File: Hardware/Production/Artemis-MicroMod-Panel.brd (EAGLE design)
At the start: 199.6 x 83.1 mm, 438 parts, among them J1 MICROMOD-2222, J10 MICROMOD-2222, J11 MICROMOD-2222, J12 MICROMOD-2222, J13 MICROMOD-2222, J14 MICROMOD-2222, J15 MICROMOD-2222, J16 MICROMOD-2222, J2 MICROMOD-2222, J3 MICROMOD-2222, J4 MICROMOD-2222, J5 MICROMOD-2222, J6 MICROMOD-2222, J7 MICROMOD-2222, J8 MICROMOD-2222, J9 MICROMOD-2222, U1 ARTEMIS_MODULESMD, U10 CH340E_MSOP10, U11 ARTEMIS_MODULESMD, U12 CH340E_MSOP10, U13 ARTEMIS_MODULESMD, U14 CH340E_MSOP10, U15 ARTEMIS_MODULESMD, U16 CH340E_MSOP10, U17 ARTEMIS_MODULESMD, U18 CH340E_MSOP10, U19 ARTEMIS_MODULESMD, U2 ARTEMIS_MODULESMD, U20 CH340E_MSOP10, U21 ARTEMIS_MODULESMD, U22 CH340E_MSOP10, U23 ARTEMIS_MODULESMD, U24 CH340E_MSOP10, U25 ARTEMIS_MODULESMD, U26 CH340E_MSOP10, U27 ARTEMIS_MODULESMD, U28 CH340E_MSOP10, U29 ARTEMIS_MODULESMD, U3 CH340E_MSOP10, U30 CH340E_MSOP10, U31 ARTEMIS_MODULESMD, U32 CH340E_MSOP10, U4 ARTEMIS_MODULESMD, U5 CH340E_MSOP10, U6 CH340E_MSOP10, U7 ARTEMIS_MODULESMD, U8 CH340E_MSOP10, U9 ARTEMIS_MODULESMD, Y1 32.768kHz, Y10 32.768kHz, Y11 32.768kHz, Y12 32.768kHz, Y13 32.768kHz, Y14 32.768kHz, Y15 32.768kHz, Y16 32.768kHz, Y2 32.768kHz, Y3 32.768kHz, Y4 32.768kHz, Y5 32.768kHz, Y6 32.768kHz, Y7 32.768kHz, Y8 32.768kHz, Y9 32.768kHz

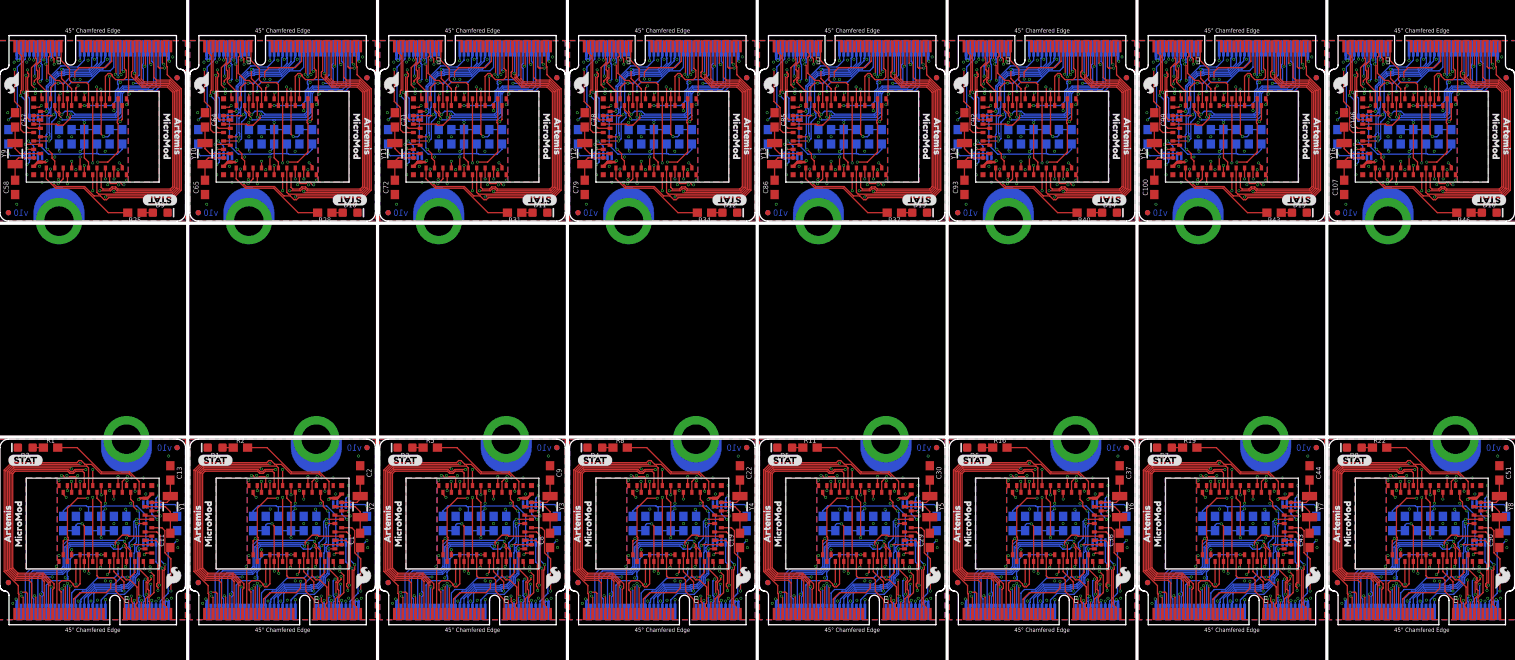
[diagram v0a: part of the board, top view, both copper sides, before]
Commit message: Adding panel files for v10
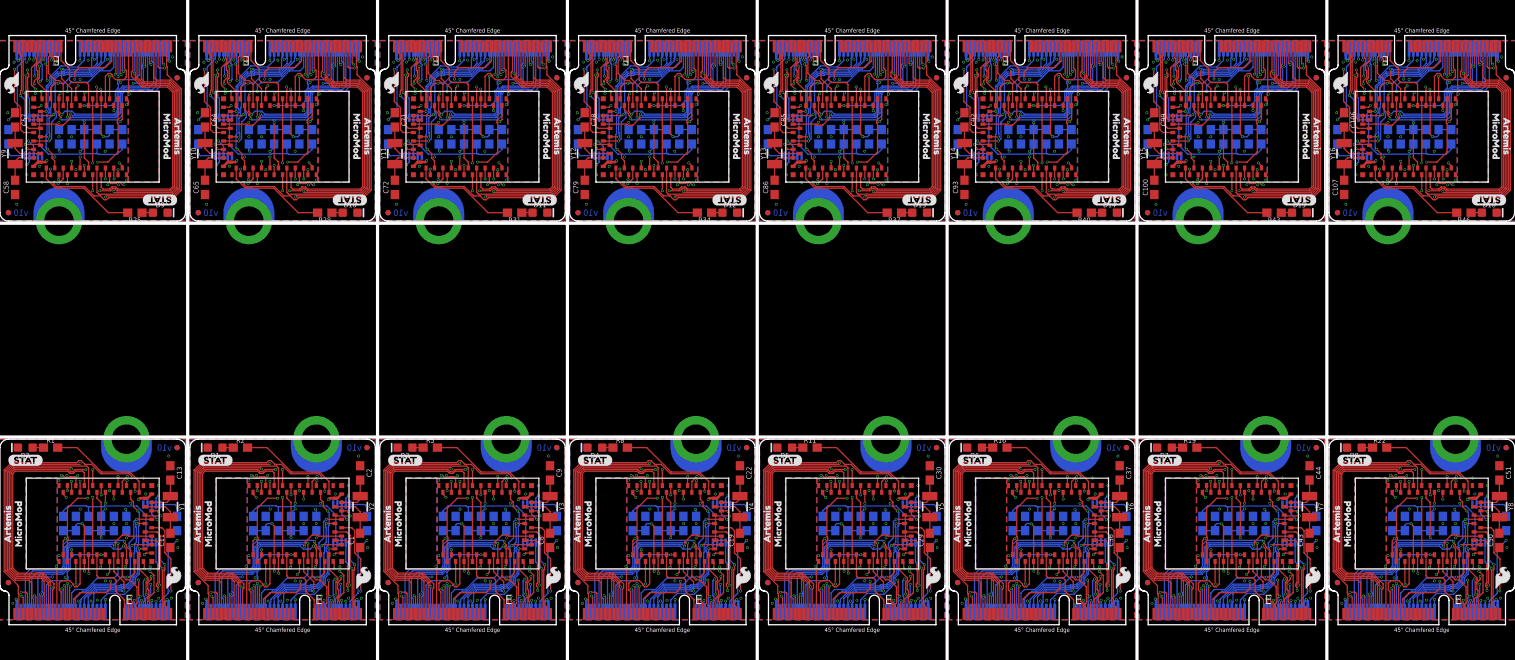
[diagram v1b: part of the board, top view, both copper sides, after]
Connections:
- net ADC_1ST renamed ADC0
- net ADC_1ST1 renamed ADC2
- net ADC_1ST10 renamed ADC20
- net ADC_1ST11 renamed ADC22
- net ADC_1ST12 renamed ADC24
- net ADC_1ST13 renamed ADC26
- net ADC_1ST14 renamed ADC28
- net ADC_1ST15 renamed ADC30
- net ADC_1ST2 renamed ADC4
- net ADC_1ST3 renamed ADC6
- net ADC_1ST4 renamed ADC8
- net ADC_1ST5 renamed ADC10
- net ADC_1ST6 renamed ADC12
- net ADC_1ST7 renamed ADC14
- net ADC_1ST8 renamed ADC16
- net ADC_1ST9 renamed ADC18
- net ADC_2ND renamed ADC1
- net ADC_2ND1 renamed ADC3
- net ADC_2ND10 renamed ADC21
- net ADC_2ND11 renamed ADC23
- net ADC_2ND12 renamed ADC25
- net ADC_2ND13 renamed ADC27
- net ADC_2ND14 renamed ADC29
- net ADC_2ND15 renamed ADC31
- net ADC_2ND2 renamed ADC5
- net ADC_2ND3 renamed ADC7
- net ADC_2ND4 renamed ADC9
- net ADC_2ND5 renamed ADC11
- net ADC_2ND6 renamed ADC13
- net ADC_2ND7 renamed ADC15
- net ADC_2ND8 renamed ADC17
- net ADC_2ND9 renamed ADC19
- net GPIO_1ST renamed D0
- net GPIO_1ST1 renamed D2
- net GPIO_1ST10 renamed D20
- net GPIO_1ST11 renamed D22
- net GPIO_1ST12 renamed D24
- net GPIO_1ST13 renamed D26
- net GPIO_1ST14 renamed D28
- net GPIO_1ST15 renamed D30
- net GPIO_1ST2 renamed D4
- net GPIO_1ST3 renamed D6
- net GPIO_1ST4 renamed D8
- net GPIO_1ST5 renamed D10
- net GPIO_1ST6 renamed D12
- net GPIO_1ST7 renamed D14
- net GPIO_1ST8 renamed D16
- net GPIO_1ST9 renamed D18
- net GPIO_2ND renamed D1
- net GPIO_2ND1 renamed D3
- net GPIO_2ND10 renamed D21
- net GPIO_2ND11 renamed D23
- net GPIO_2ND12 renamed D25
- net GPIO_2ND13 renamed D27
- net GPIO_2ND14 renamed D29
- net GPIO_2ND15 renamed D31
- net GPIO_2ND2 renamed D5
- net GPIO_2ND3 renamed D7
- net GPIO_2ND4 renamed D9
- net GPIO_2ND5 renamed D11
- net GPIO_2ND6 renamed D13
- net GPIO_2ND7 renamed D15
- net GPIO_2ND8 renamed D17
- net GPIO_2ND9 renamed D19
- net PWM_1ST renamed PWM0
- net PWM_1ST1 renamed PWM2
- net PWM_1ST10 renamed PWM20
- net PWM_1ST11 renamed PWM22
- net PWM_1ST12 renamed PWM24
- net PWM_1ST13 renamed PWM26
- net PWM_1ST14 renamed PWM28
- net PWM_1ST15 renamed PWM30
- net PWM_1ST2 renamed PWM4
- net PWM_1ST3 renamed PWM6
- net PWM_1ST4 renamed PWM8
- net PWM_1ST5 renamed PWM10
- net PWM_1ST6 renamed PWM12
- net PWM_1ST7 renamed PWM14
- net PWM_1ST8 renamed PWM16
- net PWM_1ST9 renamed PWM18
- net PWM_2ND renamed PWM1
- net PWM_2ND1 renamed PWM3
- net PWM_2ND10 renamed PWM21
- net PWM_2ND11 renamed PWM23
- net PWM_2ND12 renamed PWM25
- net PWM_2ND13 renamed PWM27
- net PWM_2ND14 renamed PWM29
- net PWM_2ND15 renamed PWM31
- net PWM_2ND2 renamed PWM5
- net PWM_2ND3 renamed PWM7
- net PWM_2ND4 renamed PWM9
- net PWM_2ND5 renamed PWM11
- net PWM_2ND6 renamed PWM13
- net PWM_2ND7 renamed PWM15
- net PWM_2ND8 renamed PWM17
- net PWM_2ND9 renamed PWM19
- removed net RTS16: J16.13, U31.D10
- removed net RX16: J16.19, U31.~D25
- removed net TX16: J16.17, U31.~D24
- new net RTS0: J2.13, U1.D10
- new net RX0: J2.19, U1.~D25
- new net TX0: J2.17, U1.~D24
- net RTS1: now also J1.13, U2.D10; no longer J2.13, U1.D10
- net RTS10: now also J11.13, U21.D10; no longer J10.13, U19.D10
- net RTS11: now also J12.13, U23.D10; no longer J11.13, U21.D10
- net RTS12: now also J13.13, U25.D10; no longer J12.13, U23.D10
- net RTS13: now also J14.13, U27.D10; no longer J13.13, U25.D10
- net RTS14: now also J15.13, U29.D10; no longer J14.13, U27.D10
- net RTS15: now also J16.13, U31.D10; no longer J15.13, U29.D10
- net RTS2: now also J3.13, U4.D10; no longer J1.13, U2.D10
- net RTS3: now also J4.13, U7.D10; no longer J3.13, U4.D10
- net RTS4: now also J5.13, U9.D10; no longer J4.13, U7.D10
- net RTS5: now also J6.13, U11.D10; no longer J5.13, U9.D10
- net RTS6: now also J7.13, U13.D10; no longer J6.13, U11.D10
- net RTS7: now also J8.13, U15.D10; no longer J7.13, U13.D10
- net RTS8: now also J9.13, U17.D10; no longer J8.13, U15.D10
- net RTS9: now also J10.13, U19.D10; no longer J9.13, U17.D10
- net RX1: now also J1.19, U2.~D25; no longer J2.19, U1.~D25
- net RX10: now also J11.19, U21.~D25; no longer J10.19, U19.~D25
- net RX11: now also J12.19, U23.~D25; no longer J11.19, U21.~D25
- net RX12: now also J13.19, U25.~D25; no longer J12.19, U23.~D25
- net RX13: now also J14.19, U27.~D25; no longer J13.19, U25.~D25
- net RX14: now also J15.19, U29.~D25; no longer J14.19, U27.~D25
- net RX15: now also J16.19, U31.~D25; no longer J15.19, U29.~D25
- net RX2: now also J3.19, U4.~D25; no longer J1.19, U2.~D25
- net RX3: now also J4.19, U7.~D25; no longer J3.19, U4.~D25
- net RX4: now also J5.19, U9.~D25; no longer J4.19, U7.~D25
- net RX5: now also J6.19, U11.~D25; no longer J5.19, U9.~D25
- net RX6: now also J7.19, U13.~D25; no longer J6.19, U11.~D25
- net RX7: now also J8.19, U15.~D25; no longer J7.19, U13.~D25
- net RX8: now also J9.19, U17.~D25; no longer J8.19, U15.~D25
- net RX9: now also J10.19, U19.~D25; no longer J9.19, U17.~D25
- net SCL1: now also J2.55, U1.D8; no longer J1.14, U2.~D39
- net SCL2: now also J1.14, U2.~D39; no longer J2.55, U1.D8
- net SDA1: now also J2.53, U1.D9; no longer J1.12, U2.D40
- net SDA2: now also J1.12, U2.D40; no longer J2.53, U1.D9
- net SPI_MOSI1: now also J2.62, U1.D7; no longer J1.59, U2.D38
- net SPI_MOSI2: now also J1.59, U2.D38; no longer J2.62, U1.D7
- net SPI_SCK1: now also J2.60, U1.~D5; no longer J1.57, U2.~D42
- net SPI_SCK2: now also J1.57, U2.~D42; no longer J2.60, U1.~D5
- net TX1: now also J1.17, U2.~D24; no longer J2.17, U1.~D24
- net TX10: now also J11.17, U21.~D24; no longer J10.17, U19.~D24
- net TX11: now also J12.17, U23.~D24; no longer J11.17, U21.~D24
- net TX12: now also J13.17, U25.~D24; no longer J12.17, U23.~D24
- net TX13: now also J14.17, U27.~D24; no longer J13.17, U25.~D24
- net TX14: now also J15.17, U29.~D24; no longer J14.17, U27.~D24
- net TX15: now also J16.17, U31.~D24; no longer J15.17, U29.~D24
- net TX2: now also J3.17, U4.~D24; no longer J1.17, U2.~D24
- net TX3: now also J4.17, U7.~D24; no longer J3.17, U4.~D24
- net TX4: now also J5.17, U9.~D24; no longer J4.17, U7.~D24
- net TX5: now also J6.17, U11.~D24; no longer J5.17, U9.~D24
- net TX6: now also J7.17, U13.~D24; no longer J6.17, U11.~D24
- net TX7: now also J8.17, U15.~D24; no longer J7.17, U13.~D24
- net TX8: now also J9.17, U17.~D24; no longer J8.17, U15.~D24
- net TX9: now also J10.17, U19.~D24; no longer J9.17, U17.~D24
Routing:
- net SPI_SCK2: track 13.0 -> 30.9 mm, vias 1 -> 0
- net SPI_SCK1: track 30.9 -> 13.0 mm, vias 0 -> 1
- net SPI_MOSI2: track 14.1 -> 31.0 mm
- net SPI_MOSI1: track 31.0 -> 14.1 mm
- net RTS16: track 14.8 -> 0.00 mm, vias 2 -> 0
- net RTS0: track 0.00 -> 14.8 mm, vias 0 -> 2
- net RX0: track 0.00 -> 10.6 mm, vias 0 -> 2
- net RX16: track 10.6 -> 0.00 mm, vias 2 -> 0
- net TX0: track 0.00 -> 8.14 mm
- net TX16: track 8.14 -> 0.00 mm
- net SCL2: track 11.7 -> 18.6 mm
- net SCL1: track 18.6 -> 11.7 mm
- net SDA2: track 10.3 -> 15.0 mm, vias 0 -> 2
- net SDA1: track 15.0 -> 10.3 mm, vias 2 -> 0

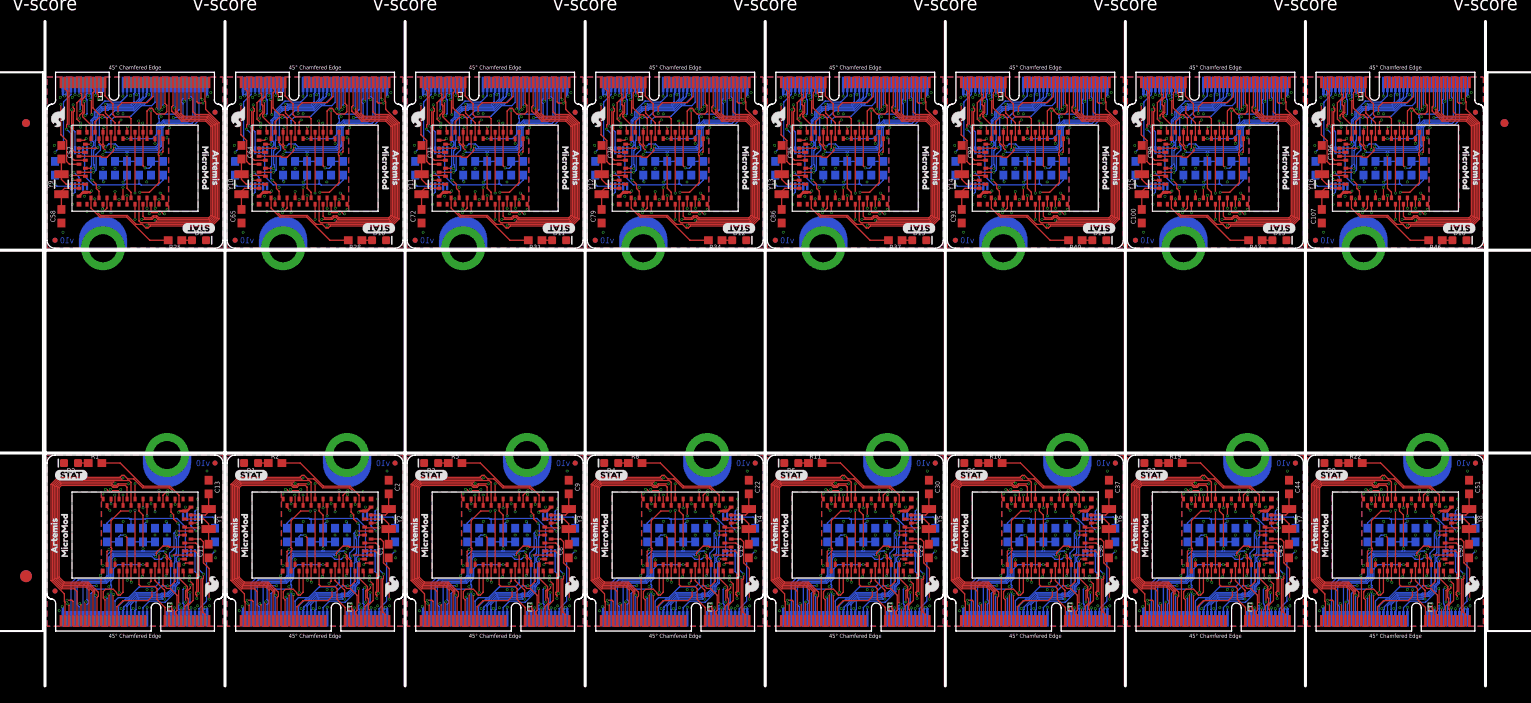
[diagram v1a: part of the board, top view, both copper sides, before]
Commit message: Routed CAM_PCLK
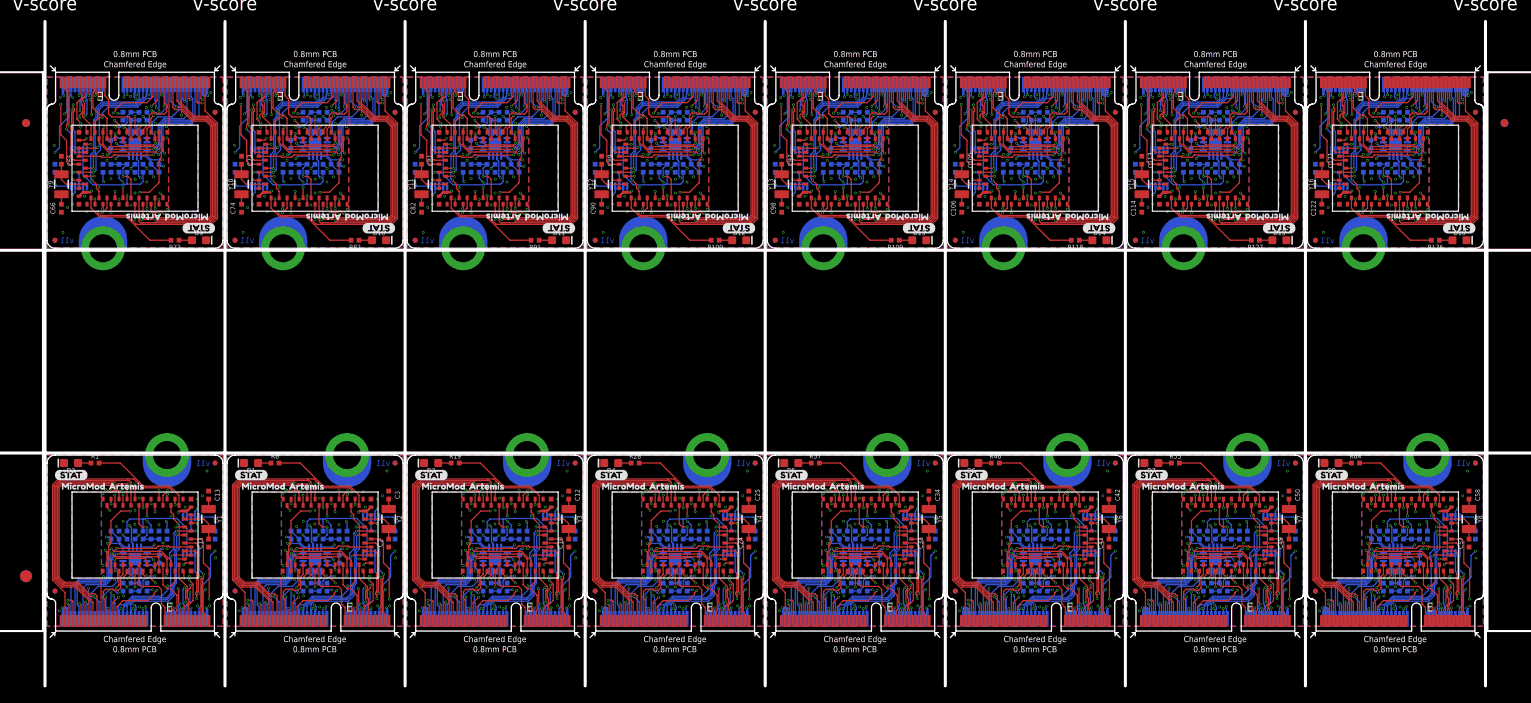
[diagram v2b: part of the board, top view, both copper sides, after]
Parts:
- removed LOGO33, LOGO36, LOGO39, LOGO42, LOGO45, LOGO48: OSHW-LOGOMINI, SparkFun-Aesthetics:OSHW-LOGO-MINI
- removed LOGO34, LOGO37, LOGO40, LOGO43, LOGO46: SFE_LOGO_NAME_FLAME.1_INCH, SparkFun-Aesthetics:SFE_LOGO_NAME_FLAME_.1
- removed LOGO35, LOGO38, LOGO41, LOGO44, LOGO47: SFE_LOGO_FLAME.1_INCH, SparkFun-Aesthetics:SFE_LOGO_FLAME_.1
- added C113, C114, C121, C122: 15pF, SparkFun-Capacitors:0402-TIGHT
- added C115, C123: 10nF, SparkFun-Capacitors:0402-TIGHT
- added C116, C117, C118, C120, C124, C125, C126, C128: 0.1uF, SparkFun-Capacitors:0402-TIGHT
- added C119, C127: 1.0nF, SparkFun-Capacitors:0402-TIGHT
- added R100, R109, R118, R127, R136, R55, R64, R73, R82, R91: 1k, SparkFun-Resistors:0402-TIGHT
- added R101, R103, R105, R107, R110, R112, R114, R116, R119, R121, R123, R125, R128, R130, R132, R134, R137, R139, R141, R143, R49, R51, R53, R56, R58, R60, R62, R65, R67, R69, R71, R74, R76, R78, R80, R83, R85, R87, R89, R92, R94, R96, R98: 100k, SparkFun-Resistors:0402-TIGHT
- added R102, R111, R120, R129, R138, R57, R66, R75, R84, R93: 220KOHM-0402T-1/16W-1%, SparkFun-Resistors:0402-TIGHT
- added R104, R106, R108, R113, R115, R117, R122, R124, R126, R131, R133, R135, R140, R142, R144, R50, R52, R54, R59, R61, R63, R68, R70, R72, R77, R79, R81, R86, R88, R90, R95, R97, R99: 150k, SparkFun-Resistors:0402-TIGHT
- added U33, U36, U39, U42, U45, U48: TSV524, OpAmp:QFN-16
- added U34, U37, U40, U43, U46: ARTEMIS_MODULESMD, SparkFun-IC-Microcontroller:ARTEMIS_FP
- added U35, U38, U41, U44, U47: CH340E_MSOP10, SparkFun-IC-Comms:MSOP10
- C1, C100, C19, C29, C30, C36, C37, C44, C64, C72, C78, C85, C86, C9, C92, C93: value 15pF -> 0.1uF; device SparkFun-Capacitors:0603 -> SparkFun-Capacitors:0402-TIGHT
- C10, C3, C66, C73: value 10nF -> 15pF; device SparkFun-Capacitors:0603 -> SparkFun-Capacitors:0402-TIGHT
- C101, C108, C23, C38, C45, C52, C80, C94: value 10nF -> 0.1uF; device SparkFun-Capacitors:0603 -> SparkFun-Capacitors:0402-TIGHT
- C102, C104, C106, C109, C11, C110, C13, C15, C17, C18, C2, C20, C21, C32, C40, C46, C48, C5, C50, C53, C54, C57, C58, C59, C6, C60, C61, C62, C65, C68, C69, C76, C88, C96: device SparkFun-Capacitors:0603 -> SparkFun-Capacitors:0402-TIGHT
- C103, C111, C39, C47, C55, C95: value 0.1uF -> 1.0nF; device SparkFun-Capacitors:0603 -> SparkFun-Capacitors:0402-TIGHT
- C105, C42, C49, C98: value 1nF -> 15pF; device SparkFun-Capacitors:0603 -> SparkFun-Capacitors:0402-TIGHT
- C107, C43, C51, C99: value 15pF -> 10nF; device SparkFun-Capacitors:0603 -> SparkFun-Capacitors:0402-TIGHT
- C112, C16, C27, C56, C7, C70, C77, C84: value 1nF -> 0.1uF; device SparkFun-Capacitors:0603 -> SparkFun-Capacitors:0402-TIGHT
- C12, C24, C25, C33, C34, C41, C74, C81, C82, C89, C90, C97: value 0.1uF -> 15pF; device SparkFun-Capacitors:0603 -> SparkFun-Capacitors:0402-TIGHT
- C14, C26, C4, C67, C75, C83: value 0.1uF -> 10nF; device SparkFun-Capacitors:0603 -> SparkFun-Capacitors:0402-TIGHT
- C22, C71, C79, C8: value 15pF -> 1.0nF; device SparkFun-Capacitors:0603 -> SparkFun-Capacitors:0402-TIGHT
- C28, C63: value 1nF -> 1.0nF; device SparkFun-Capacitors:0603 -> SparkFun-Capacitors:0402-TIGHT
- C31, C87: value 10nF -> 1.0nF; device SparkFun-Capacitors:0603 -> SparkFun-Capacitors:0402-TIGHT
- C35, C91: value 1nF -> 10nF; device SparkFun-Capacitors:0603 -> SparkFun-Capacitors:0402-TIGHT
- J1, J10, J11, J12, J13, J14, J15, J16, J2, J3, J4, J5, J6, J7, J8, J9: device Teensy:M.2-CARD-E-22 -> SparkFun-MicroMod:M.2-CARD-E-22
- LOGO11, LOGO17, LOGO2, LOGO23, LOGO29, LOGO5: value SFE_LOGO_FLAME.1_INCH -> OSHW-LOGOMINI; device SparkFun-Aesthetics:SFE_LOGO_FLAME_.1 -> SparkFun-Aesthetics:OSHW-LOGO-MINI
- LOGO12, LOGO18, LOGO24, LOGO30, LOGO6: value OSHW-LOGOMINI -> SFE_LOGO_NAME_FLAME.1_INCH; device SparkFun-Aesthetics:OSHW-LOGO-MINI -> SparkFun-Aesthetics:SFE_LOGO_NAME_FLAME_.1
- LOGO13, LOGO19, LOGO25, LOGO31, LOGO7: value SFE_LOGO_NAME_FLAME.1_INCH -> OSHW-LOGOMINI; device SparkFun-Aesthetics:SFE_LOGO_NAME_FLAME_.1 -> SparkFun-Aesthetics:OSHW-LOGO-MINI
- LOGO14, LOGO20, LOGO26, LOGO32, LOGO8: value SFE_LOGO_FLAME.1_INCH -> SFE_LOGO_NAME_FLAME.1_INCH; device SparkFun-Aesthetics:SFE_LOGO_FLAME_.1 -> SparkFun-Aesthetics:SFE_LOGO_NAME_FLAME_.1
- R1, R14, R17, R19, R20, R26, R28, R29, R3, R35, R37, R38, R44, R46, R47, R6, R8, R9: device SparkFun-Resistors:0603 -> SparkFun-Resistors:0402-TIGHT
- R10, R15, R21, R30, R39, R48: value 220k -> 220KOHM-0402T-1/16W-1%; device SparkFun-Resistors:0603 -> SparkFun-Resistors:0402-TIGHT
- R11, R2, R22, R31, R40: value 1k -> 100k; device SparkFun-Resistors:0603 -> SparkFun-Resistors:0402-TIGHT
- R12, R23, R32, R41: value 100k -> 150k; device SparkFun-Resistors:0603 -> SparkFun-Resistors:0402-TIGHT
- R13, R24, R33, R42: value 220k -> 100k; device SparkFun-Resistors:0603 -> SparkFun-Resistors:0402-TIGHT
- R16, R25, R34, R43, R5: value 1k -> 150k; device SparkFun-Resistors:0603 -> SparkFun-Resistors:0402-TIGHT
- R18, R27, R36, R4, R45, R7: value 220k -> 150k; device SparkFun-Resistors:0603 -> SparkFun-Resistors:0402-TIGHT
- U10, U16, U22, U28, U3: value CH340E_MSOP10 -> ARTEMIS_MODULESMD; device SparkFun-IC-Comms:MSOP10 -> SparkFun-IC-Microcontroller:ARTEMIS_FP
- U11, U17, U23, U29, U4: value ARTEMIS_MODULESMD -> CH340E_MSOP10; device SparkFun-IC-Microcontroller:ARTEMIS_FP -> SparkFun-IC-Comms:MSOP10
- U12, U18, U24, U30, U5: value CH340E_MSOP10 -> TSV524; device SparkFun-IC-Comms:MSOP10 -> OpAmp:QFN-16
- U15, U2, U21, U27, U9: value ARTEMIS_MODULESMD -> TSV524; device SparkFun-IC-Microcontroller:ARTEMIS_FP -> OpAmp:QFN-16
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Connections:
- removed net GPIO128: J13.48, U25.~D28
- removed net GPIO129: J13.40, U25.AD16
- removed net GPIO130: J14.73, U27.~AD29
- removed net GPIO131: J14.69, U27.D15
- removed net GPIO132: J14.71, U27.D14
- removed net GPIO133: J14.8, U27.~AD11
- removed net GPIO134: J14.67, U27.D3
- removed net GPIO135: J14.42, U27.~AD33/SWO
- removed net GPIO136: J14.46, U27.~D27
- removed net GPIO137: J14.44, U27.AD34
- removed net GPIO138: J14.48, U27.~D28
- removed net GPIO139: J14.40, U27.AD16
- removed net GPIO140: J15.73, U29.~AD29
- removed net GPIO141: J15.69, U29.D15
- removed net GPIO142: J15.71, U29.D14
- removed net GPIO143: J15.8, U29.~AD11
- removed net GPIO144: J15.67, U29.D3
- removed net GPIO145: J15.42, U29.~AD33/SWO
- removed net GPIO146: J15.46, U29.~D27
- removed net GPIO147: J15.44, U29.AD34
- removed net GPIO148: J15.48, U29.~D28
- removed net GPIO149: J15.40, U29.AD16
- removed net GPIO150: J16.73, U31.~AD29
- removed net GPIO151: J16.69, U31.D15
- removed net GPIO152: J16.71, U31.D14
- removed net GPIO153: J16.8, U31.~AD11
- removed net GPIO154: J16.67, U31.D3
- removed net GPIO155: J16.42, U31.~AD33/SWO
- removed net GPIO156: J16.46, U31.~D27
- removed net GPIO157: J16.44, U31.AD34
- removed net GPIO158: J16.48, U31.~D28
- removed net GPIO159: J16.40, U31.AD16
- removed net RTS0: J2.13, U1.D10
- removed net RX0: J2.19, U1.~D25
- removed net TX0: J2.17, U1.~D24
- new net 3.3V_EN: J1.4, U1.D3
- new net 3.3V_EN1: J2.4, U3.D3
- new net 3.3V_EN10: J11.4, U31.D3
- new net 3.3V_EN11: J12.4, U34.D3
- new net 3.3V_EN12: J13.4, U37.D3
- new net 3.3V_EN13: J14.4, U40.D3
- new net 3.3V_EN14: J15.4, U43.D3
- new net 3.3V_EN15: J16.4, U46.D3
- new net 3.3V_EN2: J3.4, U7.D3
- new net 3.3V_EN3: J4.4, U10.D3
- new net 3.3V_EN4: J5.4, U13.D3
- new net 3.3V_EN5: J6.4, U16.D3
- new net 3.3V_EN6: J7.4, U19.D3
- new net 3.3V_EN7: J8.4, U22.D3
- new net 3.3V_EN8: J9.4, U25.D3
- new net 3.3V_EN9: J10.4, U28.D3
- new net CAM_PCLK: J1.54, U1.~AD11
- new net CAM_PCLK1: J2.54, U3.~AD11
- new net CAM_PCLK10: J11.54, U31.~AD11
- new net CAM_PCLK11: J12.54, U34.~AD11
- new net CAM_PCLK12: J13.54, U37.~AD11
- new net CAM_PCLK13: J14.54, U40.~AD11
- new net CAM_PCLK14: J15.54, U43.~AD11
- new net CAM_PCLK15: J16.54, U46.~AD11
- new net CAM_PCLK2: J3.54, U7.~AD11
- new net CAM_PCLK3: J4.54, U10.~AD11
- new net CAM_PCLK4: J5.54, U13.~AD11
- new net CAM_PCLK5: J6.54, U16.~AD11
- new net CAM_PCLK6: J7.54, U19.~AD11
- new net CAM_PCLK7: J8.54, U22.~AD11
- new net CAM_PCLK8: J9.54, U25.~AD11
- new net CAM_PCLK9: J10.54, U28.~AD11
- new net N$100: D15.A, R127.1
- new net N$101: U43.XI
- new net N$102: C114.2, Y15.P$1
- new net N$103: R134.1, R135.2, U45.9
- new net N$104: R132.1, R133.2, U45.4
- new net N$105: R130.1, R131.2, U45.1
- new net N$106: C121.2, U46.XO, Y16.P$2
- new net N$107: D16.A, R136.1
- new net N$108: U46.XI
- new net N$109: C122.2, Y16.P$1
- new net N$110: R143.1, R144.2, U48.9
- new net N$111: R141.1, R142.2, U48.4
- new net N$112: R139.1, R140.2, U48.1
- new net N$49: R58.1, R59.2, U21.1
- new net N$50: C57.2, U22.XO, Y8.P$2
- new net N$51: D8.A, R64.1
- new net N$52: U22.XI
- new net N$53: C58.2, Y8.P$1
- new net N$54: R71.1, R72.2, U24.9
- new net N$55: R69.1, R70.2, U24.4
- new net N$56: R67.1, R68.2, U24.1
- new net N$57: C65.2, U25.XO, Y9.P$2
- new net N$58: D9.A, R73.1
- new net N$59: U25.XI
- new net N$60: C66.2, Y9.P$1
- new net N$61: R80.1, R81.2, U27.9
- new net N$62: R78.1, R79.2, U27.4
- new net N$63: R76.1, R77.2, U27.1
- new net N$64: C73.2, U28.XO, Y10.P$2
- new net N$65: D10.A, R82.1
- new net N$66: U28.XI
- new net N$67: C74.2, Y10.P$1
- new net N$68: R89.1, R90.2, U30.9
- new net N$69: R87.1, R88.2, U30.4
- new net N$70: R85.1, R86.2, U30.1
- new net N$71: C81.2, U31.XO, Y11.P$2
- new net N$72: D11.A, R91.1
- new net N$73: U31.XI
- new net N$74: C82.2, Y11.P$1
- new net N$75: R98.1, R99.2, U33.9
- new net N$76: R96.1, R97.2, U33.4
- new net N$77: R94.1, R95.2, U33.1
- new net N$78: C89.2, U34.XO, Y12.P$2
- new net N$79: D12.A, R100.1
- new net N$80: U34.XI
- new net N$81: C90.2, Y12.P$1
- new net N$82: R107.1, R108.2, U36.9
- new net N$83: R105.1, R106.2, U36.4
- new net N$84: R103.1, R104.2, U36.1
- new net N$85: C97.2, U37.XO, Y13.P$2
- new net N$86: D13.A, R109.1
- new net N$87: U37.XI
- new net N$88: C98.2, Y13.P$1
- new net N$89: R116.1, R117.2, U39.9
- new net N$90: R114.1, R115.2, U39.4
- new net N$91: R112.1, R113.2, U39.1
- new net N$92: C105.2, U40.XO, Y14.P$2
- new net N$93: D14.A, R118.1
- new net N$94: U40.XI
- new net N$95: C106.2, Y14.P$1
- new net N$96: R125.1, R126.2, U42.9
- new net N$97: R123.1, R124.2, U42.4
- new net N$98: R121.1, R122.2, U42.1
- new net N$99: C113.2, U43.XO, Y15.P$2
- new net RTS16: J16.13, U46.D10
- new net RX16: J16.19, U46.~D25
- new net SCALED_ADC0: U1.~AD32, U2.5, U2.6
- new net SCALED_ADC1: U1.~AD35, U2.7, U2.8
- new net SCALED_ADC10: U16.~AD32, U18.5, U18.6
- new net SCALED_ADC11: U16.~AD35, U18.7, U18.8
- new net SCALED_ADC12: U19.~AD32, U21.5, U21.6
- new net SCALED_ADC13: U19.~AD35, U21.7, U21.8
- new net SCALED_ADC14: U22.~AD32, U24.5, U24.6
- new net SCALED_ADC15: U22.~AD35, U24.7, U24.8
- new net SCALED_ADC16: U25.~AD32, U27.5, U27.6
- new net SCALED_ADC17: U25.~AD35, U27.7, U27.8
- new net SCALED_ADC18: U28.~AD32, U30.5, U30.6
- new net SCALED_ADC19: U28.~AD35, U30.7, U30.8
- new net SCALED_ADC2: U3.~AD32, U5.5, U5.6
- new net SCALED_ADC20: U31.~AD32, U33.5, U33.6
- new net SCALED_ADC21: U31.~AD35, U33.7, U33.8
- new net SCALED_ADC22: U34.~AD32, U36.5, U36.6
- new net SCALED_ADC23: U34.~AD35, U36.7, U36.8
- new net SCALED_ADC24: U37.~AD32, U39.5, U39.6
- new net SCALED_ADC25: U37.~AD35, U39.7, U39.8
- new net SCALED_ADC26: U40.~AD32, U42.5, U42.6
- new net SCALED_ADC27: U40.~AD35, U42.7, U42.8
- new net SCALED_ADC28: U43.~AD32, U45.5, U45.6
- new net SCALED_ADC29: U43.~AD35, U45.7, U45.8
- new net SCALED_ADC3: U3.~AD35, U5.7, U5.8
- new net SCALED_ADC30: U46.~AD32, U48.5, U48.6
- new net SCALED_ADC31: U46.~AD35, U48.7, U48.8
- new net SCALED_ADC4: U7.~AD32, U9.5, U9.6
- new net SCALED_ADC5: U7.~AD35, U9.7, U9.8
- new net SCALED_ADC6: U10.~AD32, U12.5, U12.6
- new net SCALED_ADC7: U10.~AD35, U12.7, U12.8
- new net SCALED_ADC8: U13.~AD32, U15.5, U15.6
- new net SCALED_ADC9: U13.~AD35, U15.7, U15.8
- new net SCALED_BATT_VIN/1: U3.~AD31, U5.15, U5.16
- new net SCALED_BATT_VIN/10: U28.~AD31, U30.15, U30.16
- new net SCALED_BATT_VIN/11: U31.~AD31, U33.15, U33.16
- new net SCALED_BATT_VIN/12: U34.~AD31, U36.15, U36.16
- new net SCALED_BATT_VIN/13: U37.~AD31, U39.15, U39.16
- new net SCALED_BATT_VIN/14: U40.~AD31, U42.15, U42.16
- new net SCALED_BATT_VIN/15: U43.~AD31, U45.15, U45.16
- new net SCALED_BATT_VIN/16: U46.~AD31, U48.15, U48.16
- new net SCALED_BATT_VIN/2: U7.~AD31, U9.15, U9.16
- new net SCALED_BATT_VIN/3: U1.~AD31, U2.15, U2.16
- new net SCALED_BATT_VIN/4: U10.~AD31, U12.15, U12.16
- new net SCALED_BATT_VIN/5: U13.~AD31, U15.15, U15.16
- new net SCALED_BATT_VIN/6: U16.~AD31, U18.15, U18.16
- new net SCALED_BATT_VIN/7: U19.~AD31, U21.15, U21.16
- new net SCALED_BATT_VIN/8: U22.~AD31, U24.15, U24.16
- new net SCALED_BATT_VIN/9: U25.~AD31, U27.15, U27.16
- new net TX16: J16.17, U46.~D24
- net !RESET!: now also J1.6; no longer J2.6
- net !RESET!1: now also C6.2, C8.1, J2.6, R9.1, U3.~RST; no longer C5.2, C7.1, J1.6, R3.1, U2.~RST
- net !RESET!10: now also C85.2, C87.1, R92.1, U31.~RST; no longer C75.2, C77.1, R32.1, U21.~RST
- net !RESET!11: now also C93.2, C95.1, R101.1, U34.~RST; no longer C82.2, C84.1, R35.1, U23.~RST
- net !RESET!12: now also C101.2, C103.1, R110.1, U37.~RST; no longer C89.2, C91.1, R38.1, U25.~RST
- net !RESET!13: now also C109.2, C111.1, R119.1, U40.~RST; no longer C96.2, C98.1, R41.1, U27.~RST
- net !RESET!14: now also C117.2, C119.1, R128.1, U43.~RST; no longer C103.2, C105.1, R44.1, U29.~RST
- net !RESET!15: now also C125.2, C127.1, R137.1, U46.~RST; no longer C110.2, C112.1, R47.1, U31.~RST
- net !RESET!2: now also C16.2, C22.1, R20.1, U7.~RST; no longer C14.2, C16.1, R6.1, U4.~RST
- net !RESET!3: now also C29.2, C31.1, R29.1, U10.~RST; no longer C25.2, C27.1, R9.1, U7.~RST
- net !RESET!4: now also C37.2, C39.1, R38.1, U13.~RST; no longer C33.2, C35.1, R12.1, U9.~RST
- net !RESET!5: now also C45.2, C47.1, R47.1, U16.~RST; no longer C40.2, C42.1, R17.1, U11.~RST
- net !RESET!6: now also C53.2, C55.1, R56.1, U19.~RST; no longer C47.2, C49.1, R20.1, U13.~RST
- net !RESET!7: now also C61.2, C63.1, R65.1, U22.~RST; no longer C54.2, C56.1, R23.1, U15.~RST
- net !RESET!8: now also C69.2, C71.1, R74.1, U25.~RST; no longer C61.2, C63.1, R26.1, U17.~RST
- net !RESET!9: now also C77.2, C79.1, R83.1, U28.~RST; no longer C68.2, C70.1, R29.1, U19.~RST
- net !RTS1: now also C7.1, U4.4; no longer C5.1, U3.4
- net !RTS10: now also C85.1, C86.1, U32.4; no longer C75.1, C76.1, U22.4
- net !RTS11: now also C93.1, C94.1, U35.4; no longer C82.1, C83.1, U24.4
- net !RTS12: now also C101.1, C102.1, U38.4; no longer C89.1, C90.1, U26.4
- net !RTS13: now also C109.1, C110.1, U41.4; no longer C96.1, C97.1, U28.4
- net !RTS14: now also C117.1, C118.1, U44.4; no longer C103.1, C104.1, U30.4
- net !RTS15: now also C125.1, C126.1, U47.4; no longer C110.1, C111.1, U32.4
- net !RTS2: now also C16.1, C19.1, U8.4; no longer C14.1, C15.1, U5.4
- net !RTS3: now also C29.1, C30.1, U11.4; no longer C25.1, C26.1, U8.4
- net !RTS4: now also C37.1, C38.1, U14.4; no longer C33.1, C34.1, U10.4
- net !RTS5: now also C45.1, C46.1, U17.4; no longer C40.1, C41.1, U12.4
- net !RTS6: now also C53.1, C54.1, U20.4; no longer C47.1, C48.1, U14.4
- net !RTS7: now also C61.1, C62.1, U23.4; no longer C54.1, C55.1, U16.4
- net !RTS8: now also C69.1, C70.1, U26.4; no longer C61.1, C62.1, U18.4
- net !RTS9: now also C77.1, C78.1, U29.4; no longer C68.1, C69.1, U20.4
- net 3.3V: now also C1.1, J1.2, J1.72, J1.74, U2.2; no longer J2.2, J2.4, J2.74
- net 3.3V1: now also C5.1, C9.1, J2.2, J2.72, J2.74, R9.2, U3.VDD@36, U3.VDD@37, U4.10, U4.7, U5.2; no longer C3.1, J1.2, J1.4, J1.74, R3.2, U2.VDD@36, U2.VDD@37, U3.10, U3.7
- net 3.3V10: now also C83.1, C84.1, C88.1, J11.72, R92.2, U31.VDD@36, U31.VDD@37, U32.10, U32.7, U33.2; no longer C73.1, C74.1, J11.4, R32.2, U21.VDD@36, U21.VDD@37, U22.10, U22.7
- net 3.3V11: now also C91.1, C92.1, C96.1, J12.72, R101.2, U34.VDD@36, U34.VDD@37, U35.10, U35.7, U36.2; no longer C80.1, C81.1, J12.4, R35.2, U23.VDD@36, U23.VDD@37, U24.10, U24.7
- net 3.3V12: now also C100.1, C104.1, C99.1, J13.72, R110.2, U37.VDD@36, U37.VDD@37, U38.10, U38.7, U39.2; no longer C87.1, C88.1, J13.4, R38.2, U25.VDD@36, U25.VDD@37, U26.10, U26.7
- net 3.3V13: now also C107.1, C108.1, C112.1, J14.72, R119.2, U40.VDD@36, U40.VDD@37, U41.10, U41.7, U42.2; no longer C94.1, C95.1, J14.4, R41.2, U27.VDD@36, U27.VDD@37, U28.10, U28.7
- net 3.3V14: now also C115.1, C116.1, C120.1, J15.72, R128.2, U43.VDD@36, U43.VDD@37, U44.10, U44.7, U45.2; no longer C101.1, C102.1, J15.4, R44.2, U29.VDD@36, U29.VDD@37, U30.10, U30.7
- net 3.3V15: now also C123.1, C124.1, C128.1, J16.72, R137.2, U46.VDD@36, U46.VDD@37, U47.10, U47.7, U48.2; no longer C108.1, C109.1, J16.4, R47.2, U31.VDD@36, U31.VDD@37, U32.10, U32.7
- net 3.3V2: now also C14.1, C15.1, C23.1, J3.72, R20.2, U7.VDD@36, U7.VDD@37, U8.10, U8.7, U9.2; no longer C10.1, C12.1, J3.4, R6.2, U4.VDD@36, U4.VDD@37, U5.10, U5.7
- net 3.3V3: now also C26.1, C27.1, C32.1, J4.72, R29.2, U10.VDD@36, U10.VDD@37, U11.10, U11.7, U12.2; no longer C23.1, C24.1, J4.4, R9.2, U7.VDD@36, U7.VDD@37, U8.10, U8.7
- net 3.3V4: now also C35.1, C36.1, C40.1, J5.72, R38.2, U13.VDD@36, U13.VDD@37, U14.10, U14.7, U15.2; no longer C31.1, C32.1, J5.4, R12.2, U10.10, U10.7, U9.VDD@36, U9.VDD@37
- net 3.3V5: now also C43.1, C44.1, C48.1, J6.72, R47.2, U16.VDD@36, U16.VDD@37, U17.10, U17.7, U18.2; no longer C38.1, C39.1, J6.4, R17.2, U11.VDD@36, U11.VDD@37, U12.10, U12.7
- net 3.3V6: now also C51.1, C52.1, C56.1, J7.72, R56.2, U19.VDD@36, U19.VDD@37, U20.10, U20.7, U21.2; no longer C45.1, C46.1, J7.4, R20.2, U13.VDD@36, U13.VDD@37, U14.10, U14.7
- net 3.3V7: now also C59.1, C60.1, C64.1, J8.72, R65.2, U22.VDD@36, U22.VDD@37, U23.10, U23.7, U24.2; no longer C52.1, C53.1, J8.4, R23.2, U15.VDD@36, U15.VDD@37, U16.10, U16.7
- net 3.3V8: now also C67.1, C68.1, C72.1, J9.72, R74.2, U25.VDD@36, U25.VDD@37, U26.10, U26.7, U27.2; no longer C59.1, C60.1, J9.4, R26.2, U17.VDD@36, U17.VDD@37, U18.10, U18.7
- net 3.3V9: now also C75.1, C76.1, C80.1, J10.72, R83.2, U28.VDD@36, U28.VDD@37, U29.10, U29.7, U30.2; no longer C66.1, C67.1, J10.4, R29.2, U19.VDD@36, U19.VDD@37, U20.10, U20.7
- net ADC0: now also J1.34, R3.2; no longer J2.34, U1.~AD32
- net ADC1: now also J1.38, R6.2; no longer J2.38, U1.~AD35
- net ADC10: now also R51.2; no longer U11.~AD32
- net ADC11: now also R53.2; no longer U11.~AD35
- net ADC12: now also R60.2; no longer U13.~AD32
- net ADC13: now also R62.2; no longer U13.~AD35
- net ADC14: now also R69.2; no longer U15.~AD32
- net ADC15: now also R71.2; no longer U15.~AD35
- net ADC16: now also R78.2; no longer U17.~AD32
- net ADC17: now also R80.2; no longer U17.~AD35
- net ADC18: now also R87.2; no longer U19.~AD32
- net ADC19: now also R89.2; no longer U19.~AD35
- net ADC2: now also J2.34, R13.2; no longer J1.34, U2.~AD32
- net ADC20: now also R96.2; no longer U21.~AD32
- net ADC21: now also R98.2; no longer U21.~AD35
- net ADC22: now also R105.2; no longer U23.~AD32
- net ADC23: now also R107.2; no longer U23.~AD35
- net ADC24: now also R114.2; no longer U25.~AD32
- net ADC25: now also R116.2; no longer U25.~AD35
- net ADC26: now also R123.2; no longer U27.~AD32
- net ADC27: now also R125.2; no longer U27.~AD35
- net ADC28: now also R132.2; no longer U29.~AD32
- net ADC29: now also R134.2; no longer U29.~AD35
- net ADC3: now also J2.38, R17.2; no longer J1.38, U2.~AD35
- net ADC30: now also R141.2; no longer U31.~AD32
- net ADC31: now also R143.2; no longer U31.~AD35
- net ADC4: now also R24.2; no longer U4.~AD32
- net ADC5: now also R26.2; no longer U4.~AD35
- net ADC6: now also R33.2; no longer U7.~AD32
- net ADC7: now also R35.2; no longer U7.~AD35
- net ADC8: now also R42.2; no longer U9.~AD32
- net ADC9: now also R44.2; no longer U9.~AD35
- net ADC_D+: now also J1.63; no longer J2.63
- net ADC_D+1: now also J2.63, U3.~AD13; no longer J1.63, U2.~AD13
- net ADC_D+10: now also U31.~AD13; no longer U21.~AD13
- net ADC_D+11: now also U34.~AD13; no longer U23.~AD13
- net ADC_D+12: now also U37.~AD13; no longer U25.~AD13
- net ADC_D+13: now also U40.~AD13; no longer U27.~AD13
- net ADC_D+14: now also U43.~AD13; no longer U29.~AD13
- net ADC_D+15: now also U46.~AD13; no longer U31.~AD13
- net ADC_D+2: now also U7.~AD13; no longer U4.~AD13
- net ADC_D+3: now also U10.~AD13; no longer U7.~AD13
- net ADC_D+4: now also U13.~AD13; no longer U9.~AD13
- net ADC_D+5: now also U16.~AD13; no longer U11.~AD13
- net ADC_D+6: now also U19.~AD13; no longer U13.~AD13
- net ADC_D+7: now also U22.~AD13; no longer U15.~AD13
- net ADC_D+8: now also U25.~AD13; no longer U17.~AD13
- net ADC_D+9: now also U28.~AD13; no longer U19.~AD13
- net ADC_D-: now also J1.65; no longer J2.65
- net ADC_D-1: now also J2.65, U3.~AD12; no longer J1.65, U2.~AD12
- net ADC_D-10: now also U31.~AD12; no longer U21.~AD12
- net ADC_D-11: now also U34.~AD12; no longer U23.~AD12
- net ADC_D-12: now also U37.~AD12; no longer U25.~AD12
- net ADC_D-13: now also U40.~AD12; no longer U27.~AD12
- net ADC_D-14: now also U43.~AD12; no longer U29.~AD12
- net ADC_D-15: now also U46.~AD12; no longer U31.~AD12
- net ADC_D-2: now also U7.~AD12; no longer U4.~AD12
- net ADC_D-3: now also U10.~AD12; no longer U7.~AD12
- net ADC_D-4: now also U13.~AD12; no longer U9.~AD12
- net ADC_D-5: now also U16.~AD12; no longer U11.~AD12
- net ADC_D-6: now also U19.~AD12; no longer U13.~AD12
- net ADC_D-7: now also U22.~AD12; no longer U15.~AD12
- net ADC_D-8: now also U25.~AD12; no longer U17.~AD12
- net ADC_D-9: now also U28.~AD12; no longer U19.~AD12
- net BATT_VIN/1: now also J2.51, R11.2; no longer J1.51, U2.~AD31
- net BATT_VIN/10: now also R85.2; no longer U19.~AD31
- net BATT_VIN/11: now also R94.2; no longer U21.~AD31
- net BATT_VIN/12: now also R103.2; no longer U23.~AD31
- net BATT_VIN/13: now also R112.2; no longer U25.~AD31
- net BATT_VIN/14: now also R121.2; no longer U27.~AD31
- net BATT_VIN/15: now also R130.2; no longer U29.~AD31
- net BATT_VIN/16: now also R139.2; no longer U31.~AD31
- net BATT_VIN/2: now also R22.2; no longer U4.~AD31
- net BATT_VIN/3: now also J1.51, R2.2; no longer J2.51, U1.~AD31
- net BATT_VIN/4: now also R31.2; no longer U7.~AD31
- net BATT_VIN/5: now also R40.2; no longer U9.~AD31
- net BATT_VIN/6: now also R49.2; no longer U11.~AD31
- net BATT_VIN/7: now also R58.2; no longer U13.~AD31
- net BATT_VIN/8: now also R67.2; no longer U15.~AD31
- net BATT_VIN/9: now also R76.2; no longer U17.~AD31
- net BOOT: now also J1.11; no longer J2.11
- net BOOT1: now also C7.2, J2.11, R10.2, U3.BOOT; no longer C6.2, J1.11, R4.2, U2.BOOT
- net BOOT10: now also C86.2, R93.2, U31.BOOT; no longer C76.2, R33.2, U21.BOOT
- net BOOT11: now also C94.2, R102.2, U34.BOOT; no longer C83.2, R36.2, U23.BOOT
- net BOOT12: now also C102.2, R111.2, U37.BOOT; no longer C90.2, R39.2, U25.BOOT
- net BOOT13: now also C110.2, R120.2, U40.BOOT; no longer C97.2, R42.2, U27.BOOT
- net BOOT14: now also C118.2, R129.2, U43.BOOT; no longer C104.2, R45.2, U29.BOOT
- net BOOT15: now also C126.2, R138.2, U46.BOOT; no longer C111.2, R48.2, U31.BOOT
- net BOOT2: now also C19.2, R21.2, U7.BOOT; no longer C15.2, R7.2, U4.BOOT
- net BOOT3: now also C30.2, R30.2, U10.BOOT; no longer C26.2, R10.2, U7.BOOT
- net BOOT4: now also C38.2, R39.2, U13.BOOT; no longer C34.2, R13.2, U9.BOOT
- net BOOT5: now also C46.2, R48.2, U16.BOOT; no longer C41.2, R18.2, U11.BOOT
- net BOOT6: now also C54.2, R57.2, U19.BOOT; no longer C48.2, R21.2, U13.BOOT
- net BOOT7: now also C62.2, R66.2, U22.BOOT; no longer C55.2, R24.2, U15.BOOT
- net BOOT8: now also C70.2, R75.2, U25.BOOT; no longer C62.2, R27.2, U17.BOOT
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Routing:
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- added copper zone on layer 15, net 3.3V
- added copper zone on layer 15, net 3.3V1
- added copper zone on layer 15, net 3.3V10
- added copper zone on layer 15, net 3.3V11
- added copper zone on layer 15, net 3.3V12
- added copper zone on layer 15, net 3.3V13
- added copper zone on layer 15, net 3.3V14
- added copper zone on layer 15, net 3.3V15
- added copper zone on layer 15, net 3.3V2
- added copper zone on layer 15, net 3.3V3
- added copper zone on layer 15, net 3.3V4
- added copper zone on layer 15, net 3.3V5
- added copper zone on layer 15, net 3.3V6
- added copper zone on layer 15, net 3.3V7
- added copper zone on layer 15, net 3.3V8
- added copper zone on layer 15, net 3.3V9
- removed copper zone on layer 2, net 3.3V
- removed copper zone on layer 2, net 3.3V1
- removed copper zone on layer 2, net 3.3V10
- removed copper zone on layer 2, net 3.3V11
- removed copper zone on layer 2, net 3.3V12
- removed copper zone on layer 2, net 3.3V13
- removed copper zone on layer 2, net 3.3V14
- removed copper zone on layer 2, net 3.3V15
- removed copper zone on layer 2, net 3.3V2
- removed copper zone on layer 2, net 3.3V3
- removed copper zone on layer 2, net 3.3V4
- removed copper zone on layer 2, net 3.3V5
- removed copper zone on layer 2, net 3.3V6
- removed copper zone on layer 2, net 3.3V7
- removed copper zone on layer 2, net 3.3V8
- removed copper zone on layer 2, net 3.3V9
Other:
- board text added: "v11"
- board text removed: "45° Chamfered Edge"
- board text removed: "v10"
